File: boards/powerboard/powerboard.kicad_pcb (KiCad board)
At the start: 2 copper layers, 97.2 x 68.6 mm, 211 parts, among them J101 RXSM experiment connector, J102 Powerboard <-> Mainboard, J103 Cameraboard, J104 BLDC Motor, J105 BOOST, J106 Boost24V_EN, J107 24V_1, J108 24V_2, J109 24V_3, J110 BAT, J111 GND, J112 M3, J113 M3, J114 M3, J115 M3, J116 M3, J117 M3, J118 M3, J119 GND, J801 Heat probe power, P501 10k NTC, Q101 SQM40031EL, Q102 DMN6140L, Q104 DMN6140L, Q501 DMN6140L, Q502 PMV27UPE, Q503 IRF7343PBF, Q801 BUK7Y4R8-60E, Q802 BUK7Y4R8-60E, Q803 BUK7Y4R8-60E, U1001 LT3592, U101 LM1117-3.3, U102 DS26LV32AT, U1101 LMV324, U1102 LMV324, U201 LMZ14203, U301 LM3480-12, U302 DRV8332, U303 ACS711, U501 LTC4010, U601 PC3H7, U602 PC3H7, U603 PC3H7, U701 MAX13432EESD, U801 ACS711, U802 ACS711, U803 ACS711, U901 AD7928, U902 REF3025

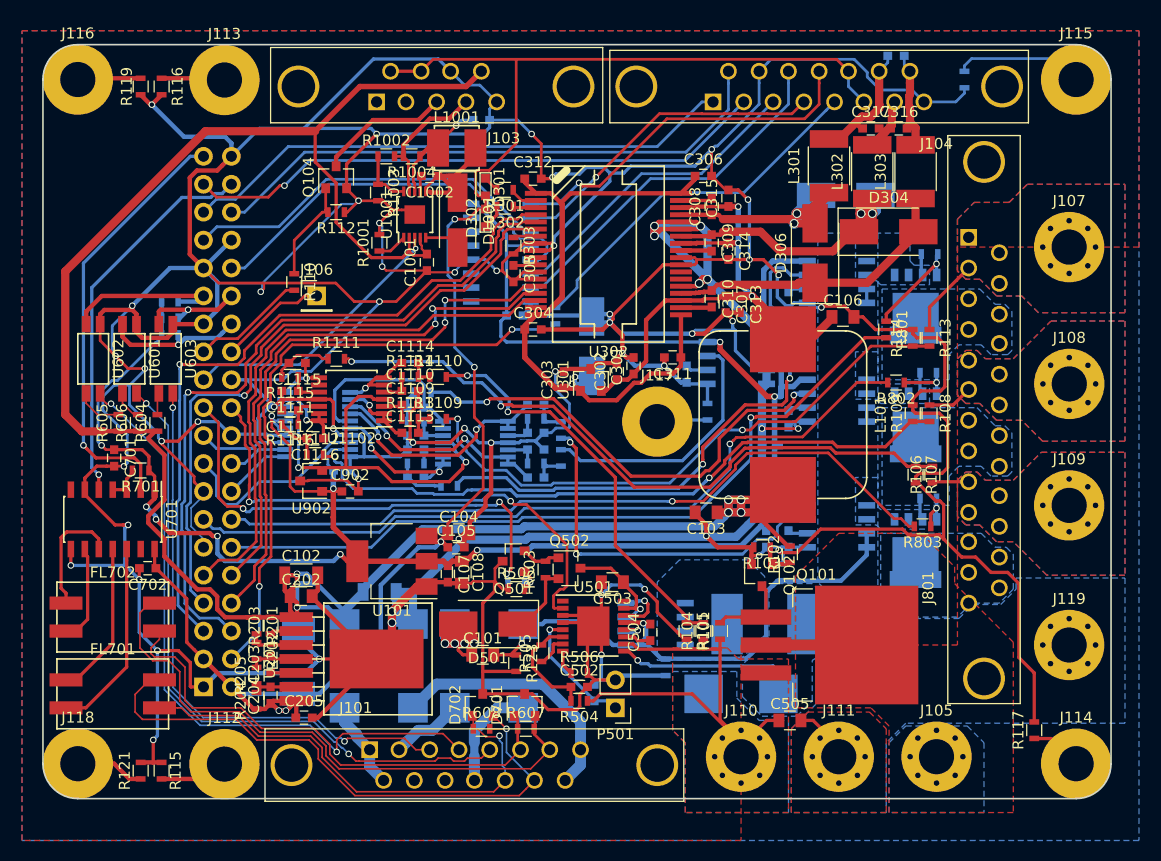
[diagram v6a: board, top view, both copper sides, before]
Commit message: [powerboard] silkscreen and ground plane
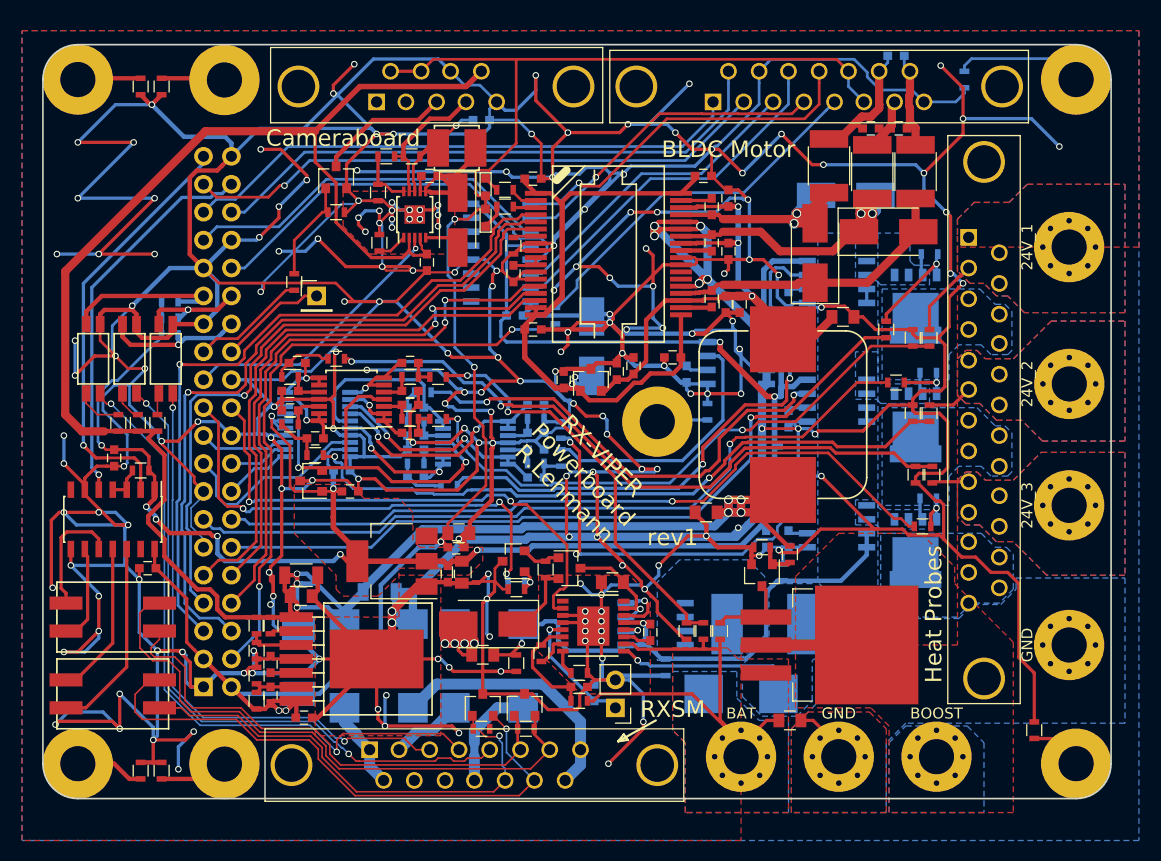
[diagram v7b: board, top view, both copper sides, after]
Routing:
- net GND: track 873.9 -> 1485.8 mm, vias 53 -> 191
- net Net-(U302-Pad23): track 40.5 -> 36.3 mm
- net GNDPWR: track 61.1 -> 62.4 mm
- net /Hall_U: track 50.5 -> 51.2 mm
- net /RX: track 39.8 -> 39.1 mm
- added copper zone on F.Cu, net +3V3
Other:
- board text added: "Heat Probes"
- board text added: "RX-VIPER Powerboard R.Lehmann"
- board text added: "RXSM"
- board text added: "rev1"

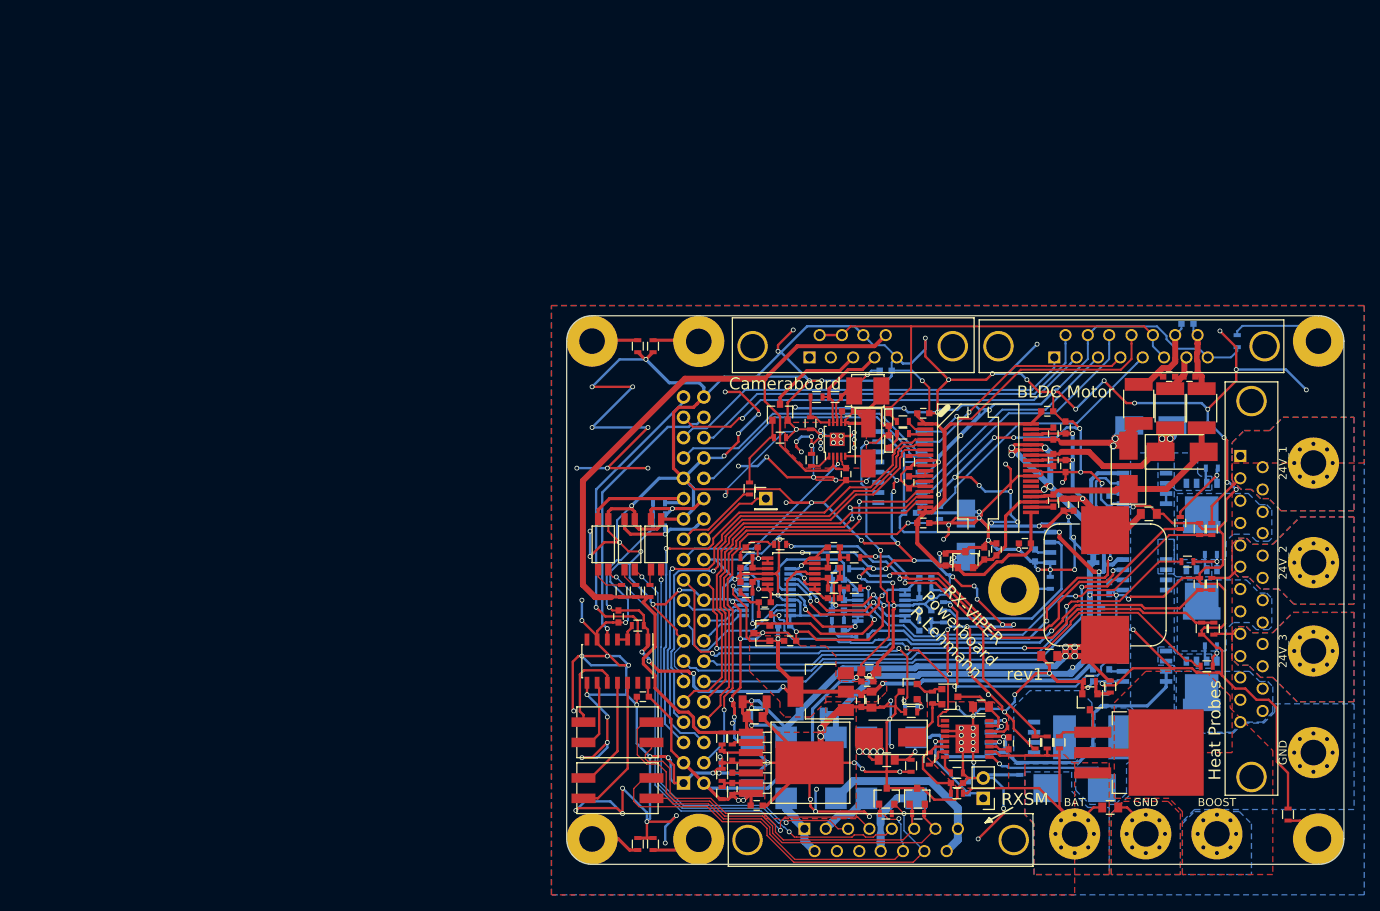
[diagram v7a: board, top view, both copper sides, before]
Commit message: [powerboard] export layout
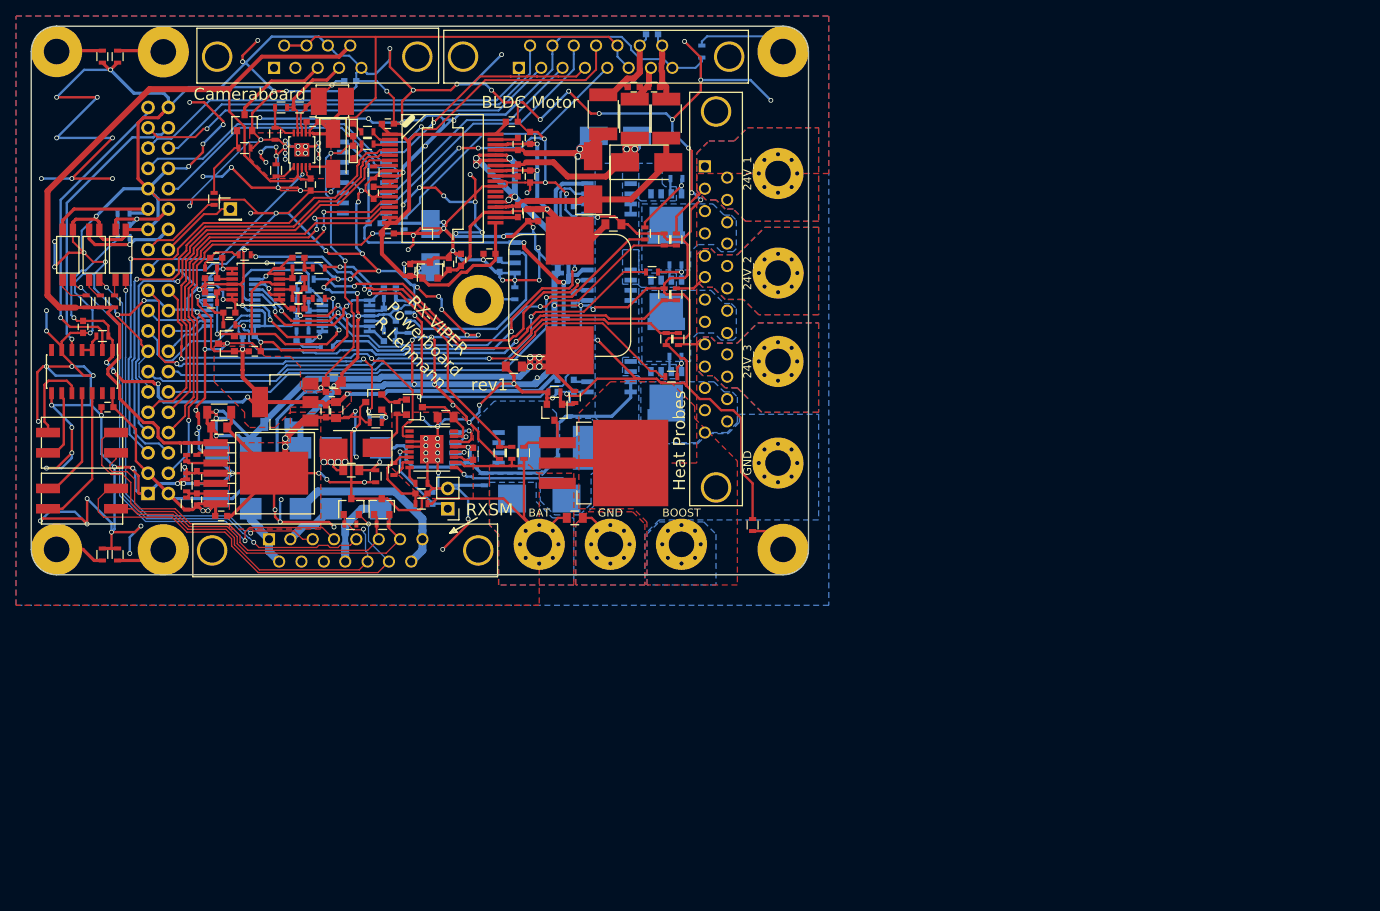
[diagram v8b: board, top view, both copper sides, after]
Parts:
- moved C1002 76.1 mm to (84.4, 35.4)
- moved C104 76.1 mm to (87.1, 67.9)
- moved C108 76.1 mm to (87.4, 71.5)
- moved C1111 76.1 mm to (71.8, 55.0)
- moved C1116 76.1 mm to (74.0, 59.3)
- moved C201 76.1 mm to (79.9, 73.3)
- moved C203 76.1 mm to (70.0, 79.9)
- moved C304 76.1 mm to (93.9, 49.4)
- moved C306 76.1 mm to (109.3, 35.4)
- moved C308 76.1 mm to (110.1, 38.2)
- moved C309 76.1 mm to (110.1, 41.5)
- moved C310 76.1 mm to (110.1, 46.6)
- moved C311 76.1 mm to (106.6, 51.9)
- moved C312 76.1 mm to (93.9, 35.7)
- moved C314 76.1 mm to (111.6, 42.3)
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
